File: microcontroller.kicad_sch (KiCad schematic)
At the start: 45 parts, among them J5 USB4105-GF-A, J7 DEBUG, U2 W25Q32JV, U3 RP2350A, U4 MCP1702T-3302E_CB, X1 IQXO-791

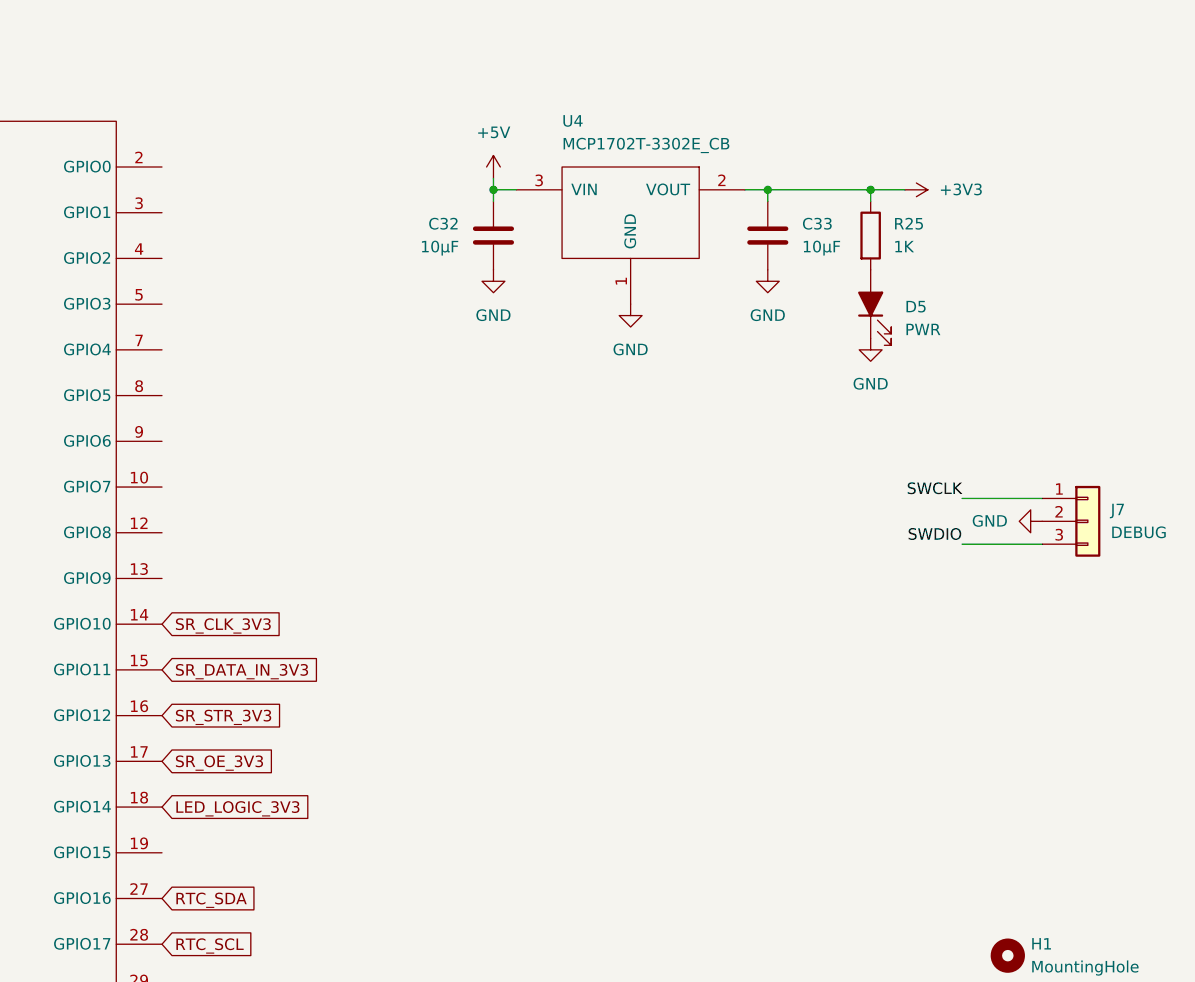
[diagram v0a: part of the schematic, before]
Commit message: Fix 3V3/+3V3 nets; update pinouts for easier routing
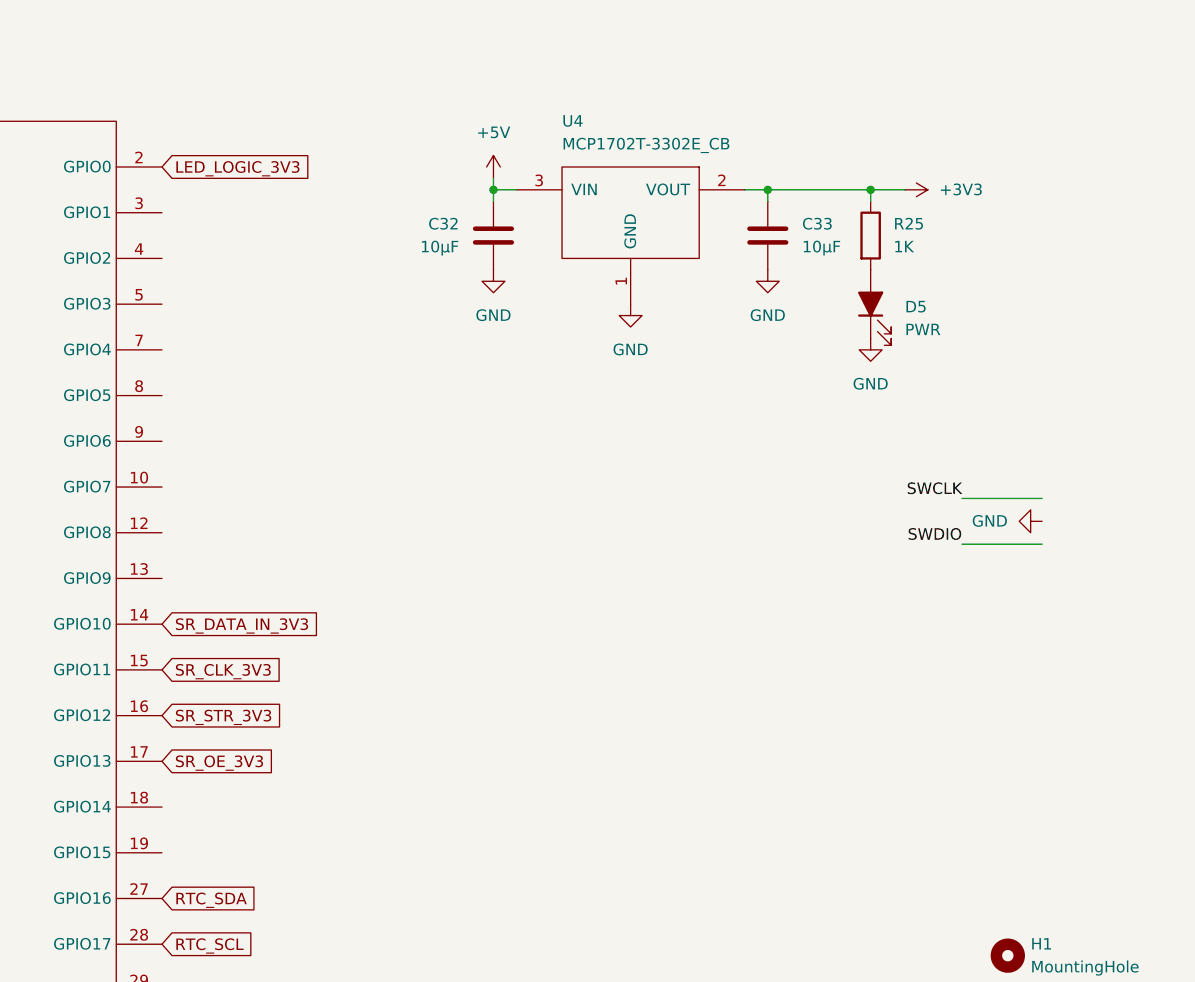
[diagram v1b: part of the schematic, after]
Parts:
- removed J7: DEBUG, Connector_PinHeader_2.54mm:PinHeader_1x03_P2.54mm_Vertical, symbol Connector_Generic:Conn_01x03
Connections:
- net LED_LOGIC_3V3: now also U3.2 (GPIO0); no longer U3.18 (GPIO14)
- net SR_CLK_3V3: now also U3.15 (GPIO11); no longer U3.14 (GPIO10)
- net SR_DATA_IN_3V3: now also U3.14 (GPIO10); no longer U3.15 (GPIO11)
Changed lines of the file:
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@@
 	(global_label "SR_CLK_3V3"
 		(shape input)
-		(at 167.64 77.47 0)
+		(at 167.64 82.55 0)
 		(fields_autoplaced yes)
 		(effects
@@
 		)
 		(property "Intersheetrefs" "${INTERSHEET_REFS}"
-			(at 182.1156 77.47 0)
+			(at 182.1156 82.55 0)
 			(effects
 				(font
@@
 	(global_label "SR_DATA_IN_3V3"
 		(shape input)
-		(at 167.64 82.55 0)
+		(at 167.64 77.47 0)
 		(fields_autoplaced yes)
 		(effects
@@
 		)
 		(property "Intersheetrefs" "${INTERSHEET_REFS}"
-			(at 185.8652 82.55 0)
+			(at 185.8652 77.47 0)
 			(effects
 				(font
@@
 	(global_label "LED_LOGIC_3V3"
 		(shape input)
-		(at 167.64 97.79 0)
+		(at 167.64 26.67 0)
 		(fields_autoplaced yes)
 		(effects
@@
 		)
 		(property "Intersheetrefs" "${INTERSHEET_REFS}"
-			(at 185.0185 97.79 0)
+			(at 185.0185 26.67 0)
 			(effects
 				(font
@@
 					(unit 1)
 				)
-			)
-		)
-	)
-	(symbol
-		(lib_id "Connector_Generic:Conn_01x03")
-		(at 270.51 66.04 0)
-		(unit 1)
-		(exclude_from_sim no)
-		(in_bom yes)
-		(on_board yes)
-		(dnp no)
-		(fields_autoplaced yes)
-		(property "Reference" "J7"
-			(at 273.05 64.7699 0)
-			(effects
-				(font
-					(size 1.27 1.27)
-				)
-				(justify left)
-			)
-		)
-		(property "Value" "DEBUG"
-			(at 273.05 67.3099 0)
-			(effects
-				(font
-					(size 1.27 1.27)
-				)
-				(justify left)
-			)
-		)
-		(property "Footprint" "Connector_PinHeader_2.54mm:PinHeader_1x03_P2.54mm_Vertical"
-			(at 270.51 66.04 0)
-			(effects
-				(font
-					(size 1.27 1.27)
-				)
-				(hide yes)
-			)
-		)
-		(property "Datasheet" "~"
-			(at 270.51 66.04 0)
-			(effects
-				(font
-					(size 1.27 1.27)
-				)
-				(hide yes)
-			)
-		)
-		(property "Description" ""
-			(at 270.51 66.04 0)
-			(effects
-				(font
-					(size 1.27 1.27)
-				)
-			)
-		)
-		(property "DigiKeyPN" ""
-			(at 270.51 66.04 0)
-			(effects
-				(font
-					(size 1.27 1.27)
-				)
-				(hide yes)
-			)
-		)
-		(pin "1"
-		)
-		(pin "2"
-		)
-		(pin "3"
-		)
-		(instances
-			(project "nixie-tube-clock"
-				(path "/a9820232-e60b-442f-bf19-e58448ec1fae/c3042731-628e-4c53-9276-3a8f19129a46"
-					(reference "J7")
-					(unit 1)
-				)

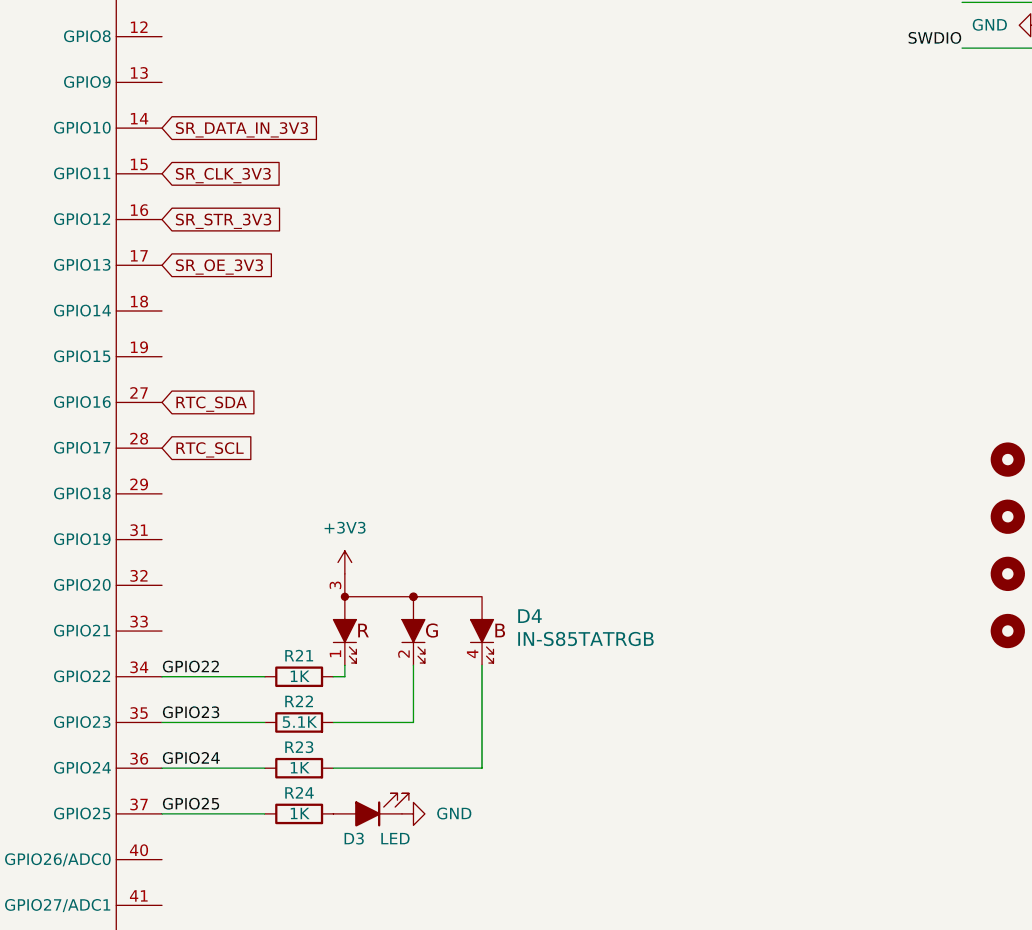
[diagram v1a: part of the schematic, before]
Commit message: Add time set buttons
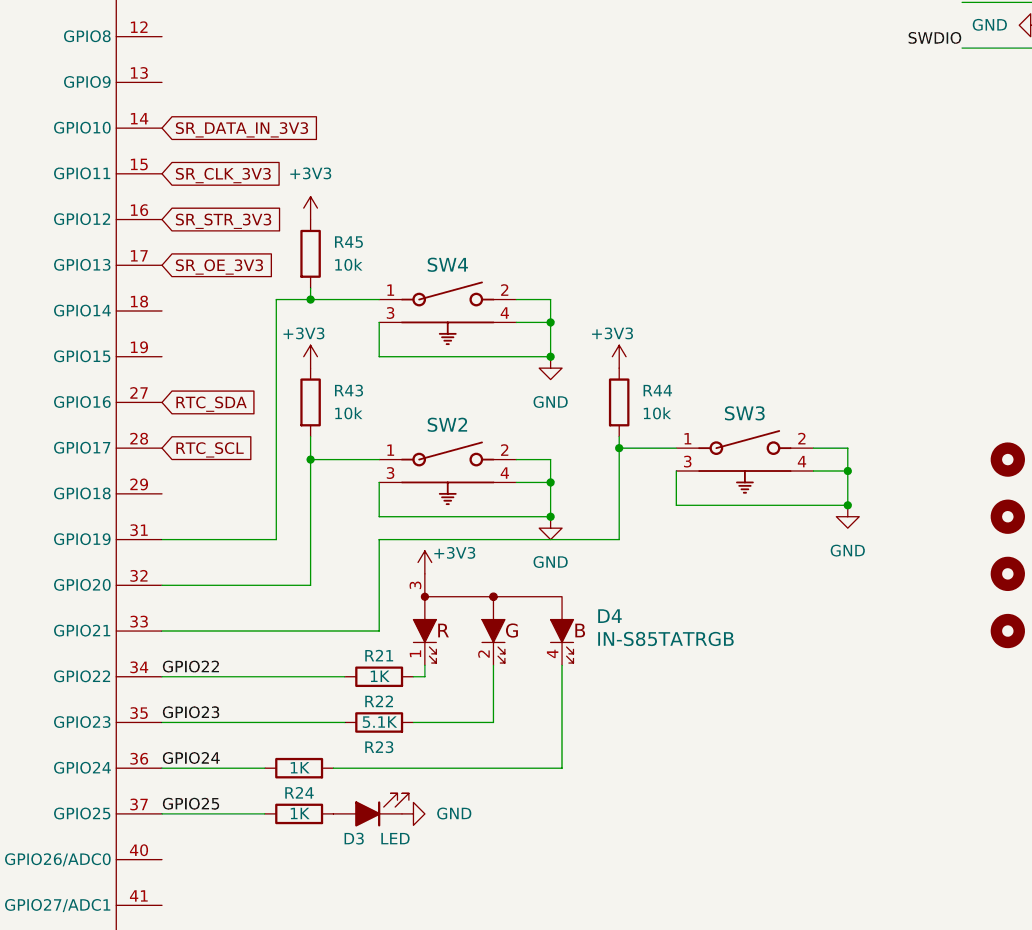
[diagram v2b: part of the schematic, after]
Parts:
- added R43, R44, R45: 10k, Resistor_SMD:R_0603_1608Metric, symbol Device:R
- added SW2, SW3, SW4: 1825027-8, carter_kicad_footprints:SW2_1825027-C_TEC, symbol carter_kicad_symbols:1825027-8 Right Angle Button
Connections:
- net +3V3: now also R43.1, R44.1, R45.1
- net GND: now also SW2.2, SW2.3, SW2.4, SW3.2, SW3.3, SW3.4, SW4.2, SW4.3, SW4.4
- net at U3.31 (GPIO19): now also R45.2, SW4.1
- net at U3.32 (GPIO20): now also R43.2, SW2.1
- net at U3.33 (GPIO21): now also R44.2, SW3.1
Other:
- moved on the sheet: D4, R21, R22

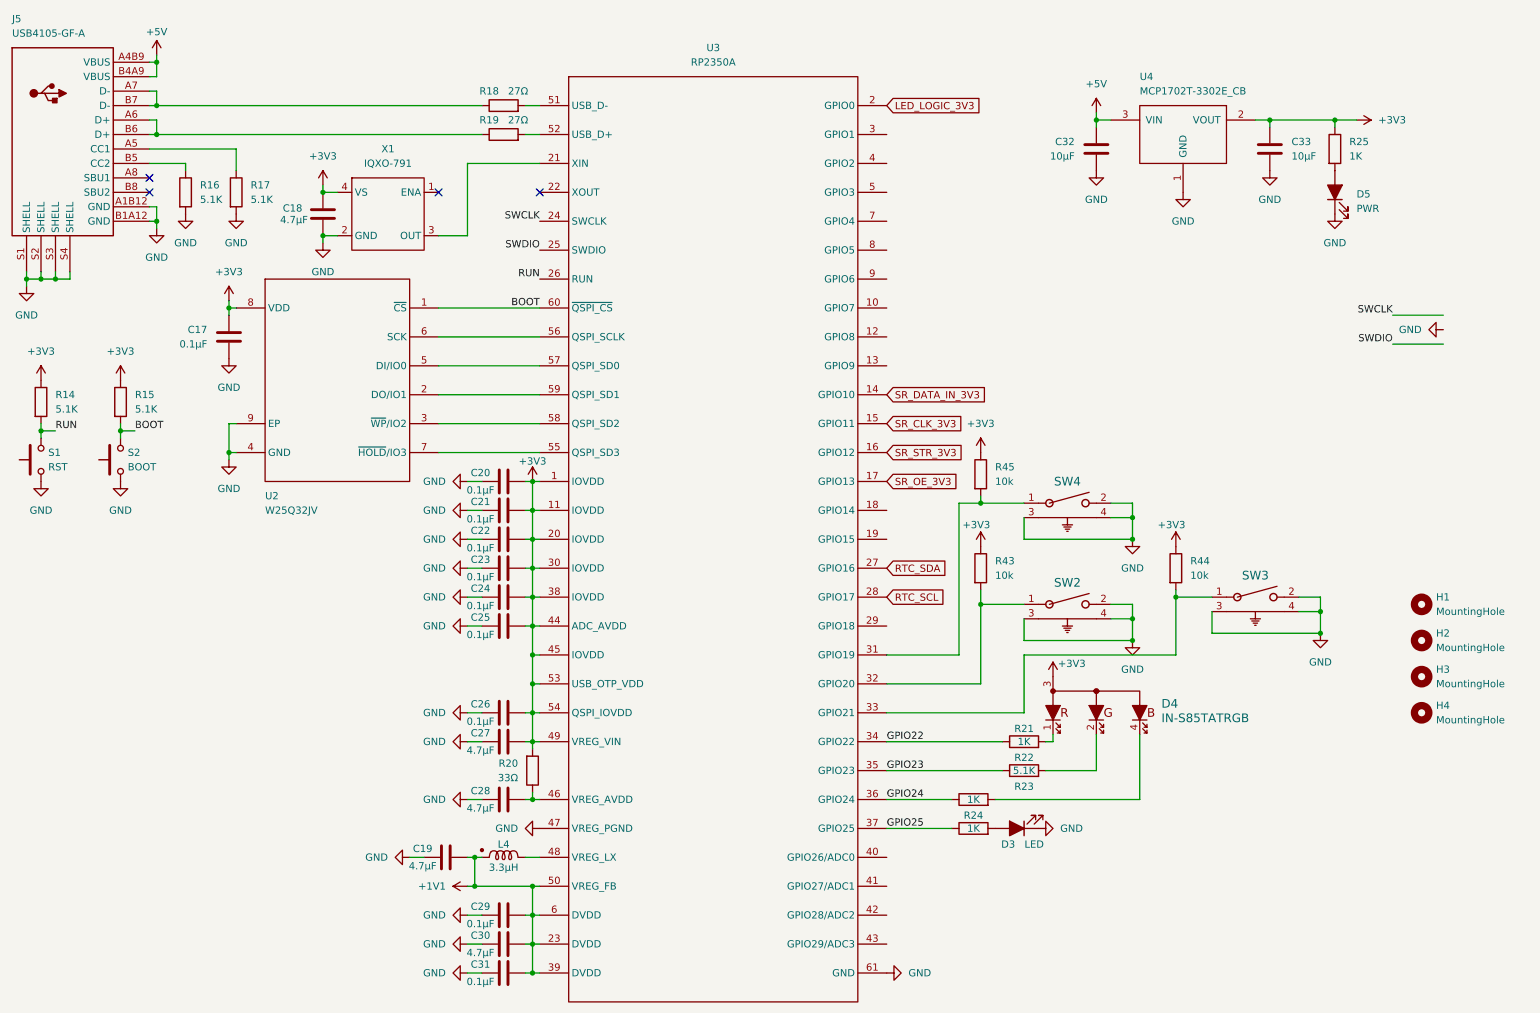
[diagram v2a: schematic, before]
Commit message: BOM simplification of redundant components
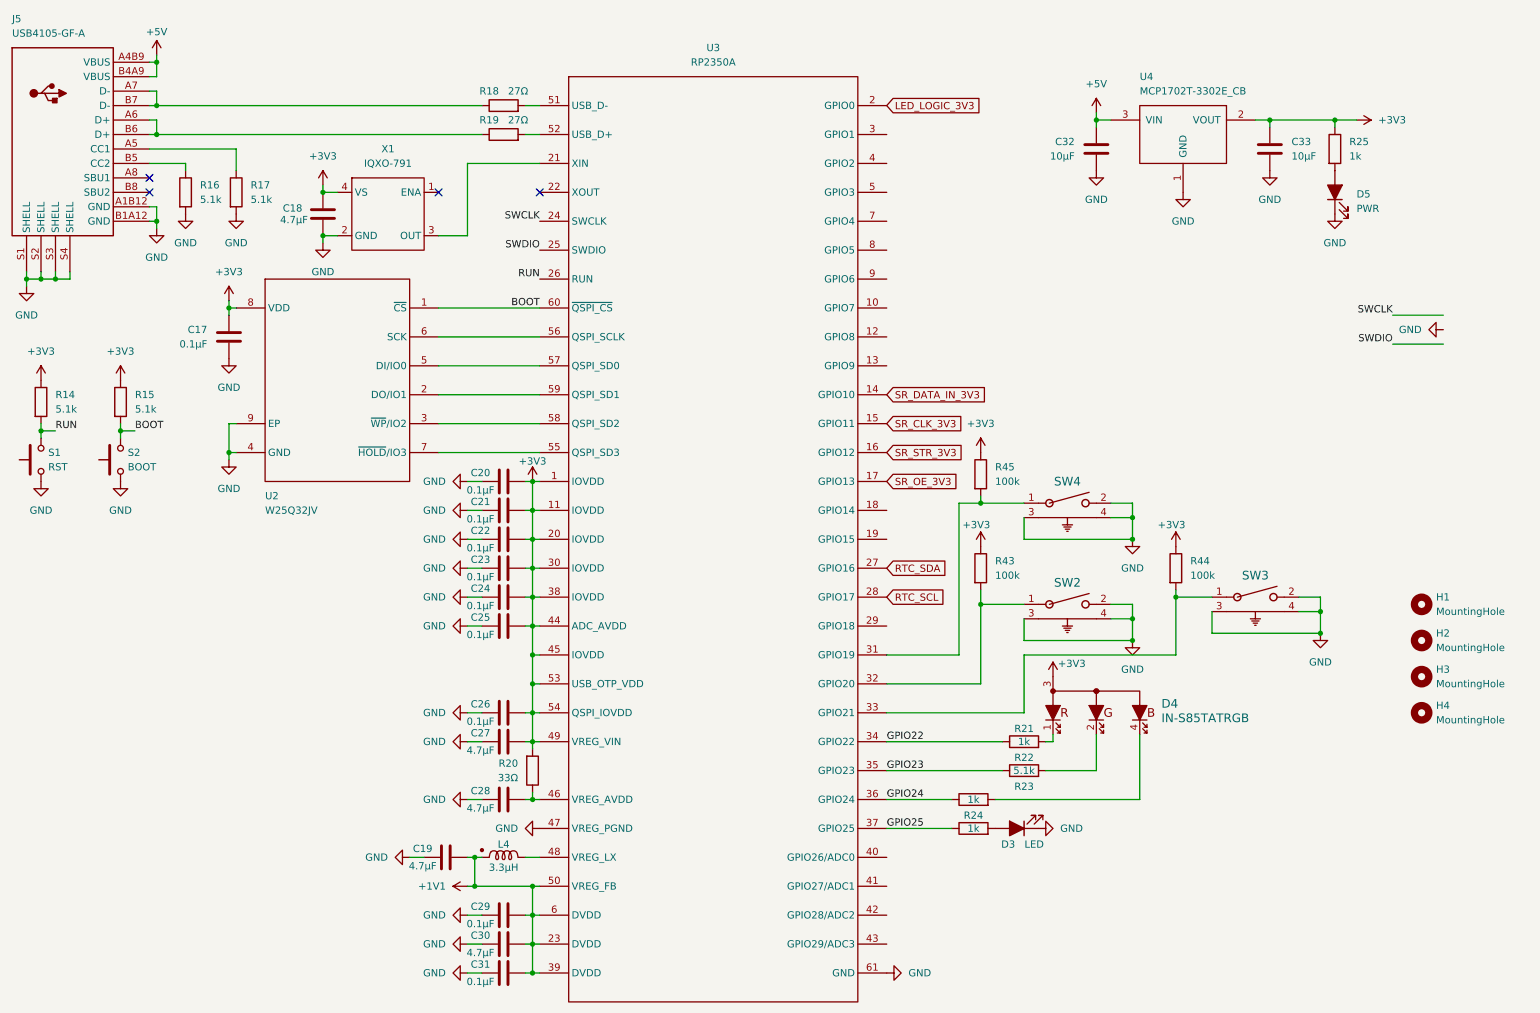
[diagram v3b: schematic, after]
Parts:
- R14, R15, R16, R17, R22: value 5.1K -> 5.1k
- R21, R23, R24, R25: value 1K -> 1k
- R43, R44, R45: value 10k -> 100k

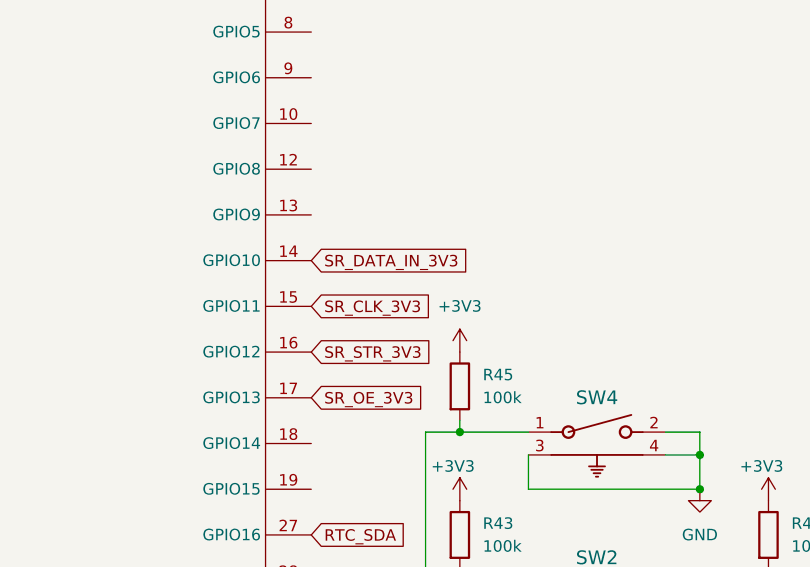
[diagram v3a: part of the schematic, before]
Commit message: Fix misplacement of spi tx and clk pins
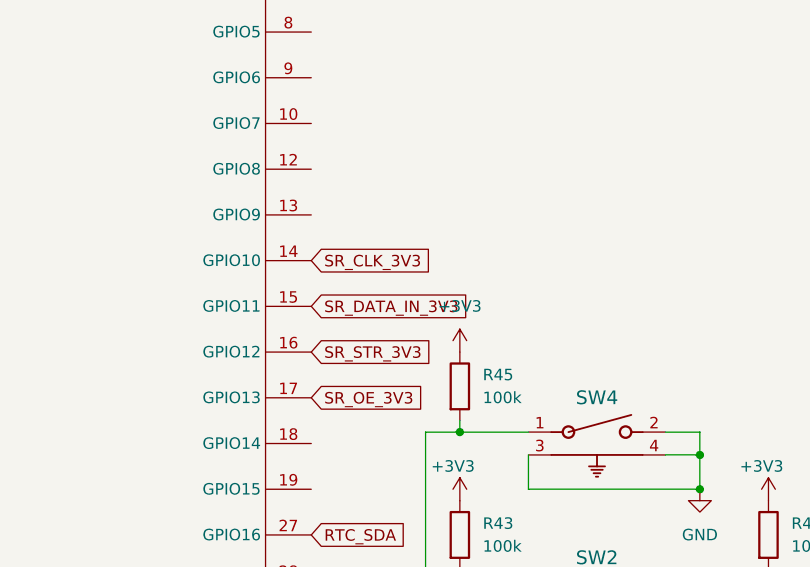
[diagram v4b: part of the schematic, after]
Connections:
- net SR_CLK_3V3: now also U3.14 (GPIO10); no longer U3.15 (GPIO11)
- net SR_DATA_IN_3V3: now also U3.15 (GPIO11); no longer U3.14 (GPIO10)
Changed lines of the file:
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@@
 	(global_label "SR_CLK_3V3"
 		(shape input)
-		(at 167.64 82.55 0)
+		(at 167.64 77.47 0)
 		(fields_autoplaced yes)
 		(effects
@@
 		)
 		(property "Intersheetrefs" "${INTERSHEET_REFS}"
-			(at 182.1156 82.55 0)
+			(at 182.1156 77.47 0)
 			(effects
 				(font
@@
 	(global_label "SR_DATA_IN_3V3"
 		(shape input)
-		(at 167.64 77.47 0)
+		(at 167.64 82.55 0)
 		(fields_autoplaced yes)
 		(effects
@@
 		)
 		(property "Intersheetrefs" "${INTERSHEET_REFS}"
-			(at 185.8652 77.47 0)
+			(at 185.8652 82.55 0)
 			(effects
 				(font
